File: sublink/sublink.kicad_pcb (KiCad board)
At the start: 2 copper layers, 21 parts

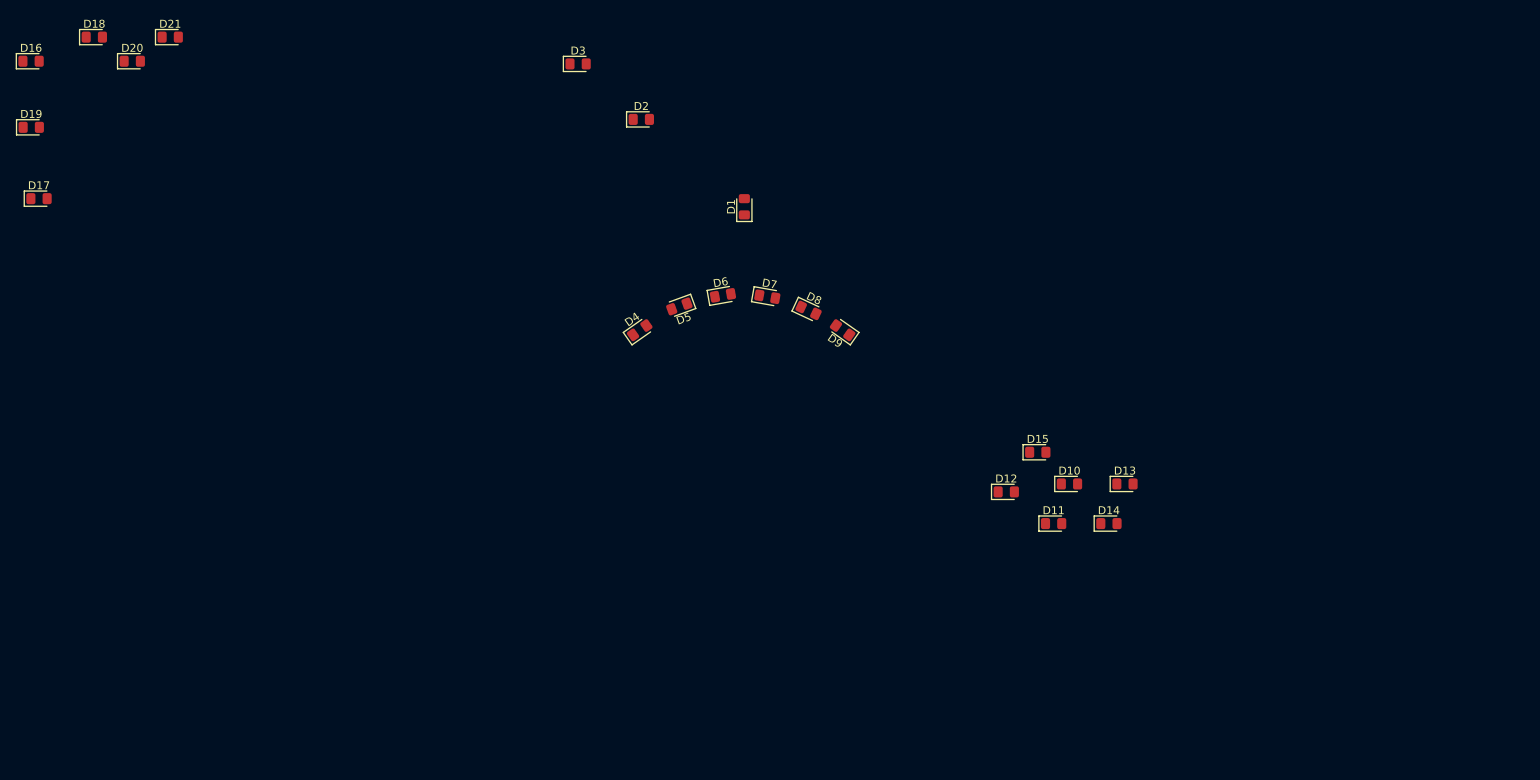
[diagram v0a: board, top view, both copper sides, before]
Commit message: wip board outline, led placement
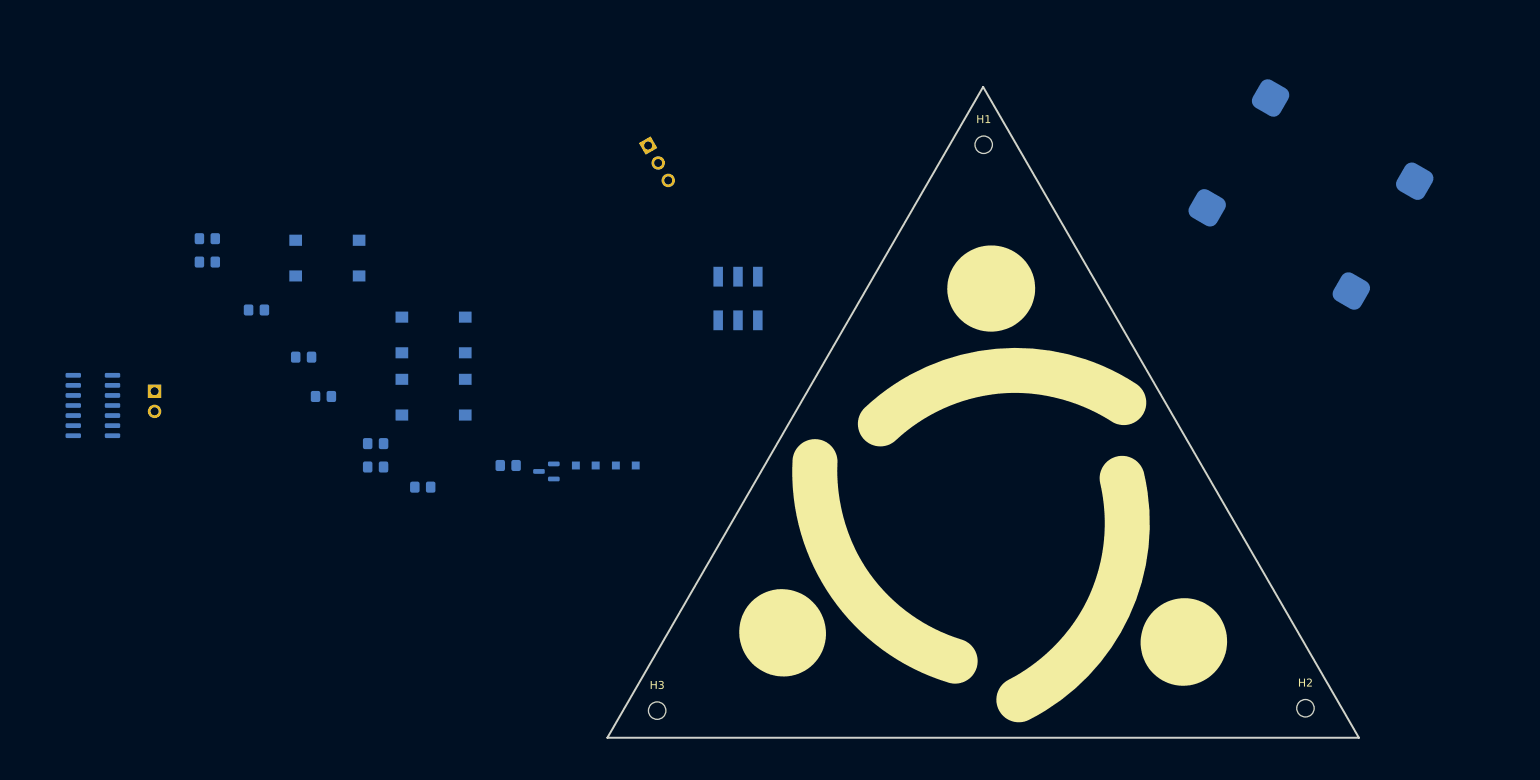
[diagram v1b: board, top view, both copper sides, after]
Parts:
- added BT1: 3V7, Connector_PinHeader_2.54mm:PinHeader_1x02_P2.54mm_Vertical, B.Cu at (68.6, 83.3)
- added D22: DNP, Diode_SMD:D_SOD-323_HandSoldering, B.Cu at (123.0, 92.7)
- added D23: BAS21HT1G, Diode_SMD:D_SOD-323_HandSoldering, B.Cu at (128.0, 92.7)
- added H1: MountingHole, MountingHole:MountingHole_2.2mm_M2, F.Cu at (173.2, 52.2)
- added H2: MountingHole, MountingHole:MountingHole_2.2mm_M2, F.Cu at (213.8, 123.3)
- added H3: MountingHole, MountingHole:MountingHole_2.2mm_M2, F.Cu at (132.0, 123.6)
- added J1: Conn_01x03_Female, Connector_PinSocket_2.54mm:PinSocket_1x03_P2.54mm_Horizontal, B.Cu at (130.9, 52.3)
- added Q1: YJL2305A, Package_TO_SOT_SMD:SOT-23, B.Cu at (118.0, 93.4)
- added R1: R_Small, Resistor_SMD:R_0805_2012Metric_Pad1.20x1.40mm_HandSolder, B.Cu at (75.2, 67.0)
- added R2: R_Small, Resistor_SMD:R_0805_2012Metric_Pad1.20x1.40mm_HandSolder, B.Cu at (96.5, 89.9)
- added R3: R_Small, Resistor_SMD:R_0805_2012Metric_Pad1.20x1.40mm_HandSolder, B.Cu at (102.4, 95.4)
- added R4: R_Small, Resistor_SMD:R_0805_2012Metric_Pad1.20x1.40mm_HandSolder, B.Cu at (113.2, 92.7)
- added R5: R_Small, Resistor_SMD:R_0805_2012Metric_Pad1.20x1.40mm_HandSolder, B.Cu at (89.9, 84.0)
- added R6: R_Small, Resistor_SMD:R_0805_2012Metric_Pad1.20x1.40mm_HandSolder, B.Cu at (75.2, 64.0)
- added R7: R_Small, Resistor_SMD:R_0805_2012Metric_Pad1.20x1.40mm_HandSolder, B.Cu at (81.4, 73.0)
- added R8: R_Small, Resistor_SMD:R_0805_2012Metric_Pad1.20x1.40mm_HandSolder, B.Cu at (96.5, 92.9)
- added R9: 10k, Resistor_SMD:R_0805_2012Metric_Pad1.20x1.40mm_HandSolder, B.Cu at (87.4, 79.0)
- added SW1: SW_Push, Button_Switch_SMD:SW_SPST_Omron_B3FS-100xP, B.Cu at (103.8, 76.2)
- added SW2: SW_Push, Button_Switch_SMD:SW_SPST_Omron_B3FS-100xP, B.Cu at (90.4, 66.5)
- added SW3: SW_Push, Button_Switch_SMD:SW_SPST_Omron_B3FS-100xP, B.Cu at (103.8, 84.0)
- added U1: ATtiny414-SS, Package_SO:SOIC-14_3.9x8.7mm_P1.27mm, B.Cu at (60.8, 85.1)
- added U2: OKY3402, sublink_custom:OKY3402, B.Cu at (214.5, 58.5)
- added U3: JS202011, sublink_custom:JS202011, B.Cu at (142.2, 71.6)
- moved D16 138.8 mm to (169.2, 117.6), turned to -20 degrees
- moved D17 122.7 mm to (163.3, 114.6), turned to -35 degrees
- moved D18 121.0 mm to (158.4, 110.4), turned to -50 degrees
- moved D19 115.5 mm to (154.7, 104.9), turned to -65 degrees
- moved D20 103.8 mm to (152.4, 98.9), turned to -80 degrees
- moved D21 97.3 mm to (151.7, 92.4), turned to -90 degrees
- moved D2 95.1 mm to (198.4, 115.0), turned to -25 degrees
- moved D3 76.2 mm to (147.8, 113.8), turned to -140 degrees
- moved D9 36.5 mm to (190.9, 84.2), turned to 150 degrees
- moved D8 34.8 mm to (184.8, 81.6), turned to 160 degrees
- moved D7 33.7 mm to (178.3, 80.7), turned to 180 degrees
- moved D6 33.1 mm to (171.9, 81.2), turned to -170 degrees
- moved D1 32.9 mm to (174.2, 70.3)
- moved D5 32.7 mm to (165.7, 83.4), turned to -155 degrees
- moved D4 32.6 mm to (160.3, 87.1), turned to -140 degrees
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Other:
- board outline added: 94.8 x 82.1 mm

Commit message: first pass all components placement
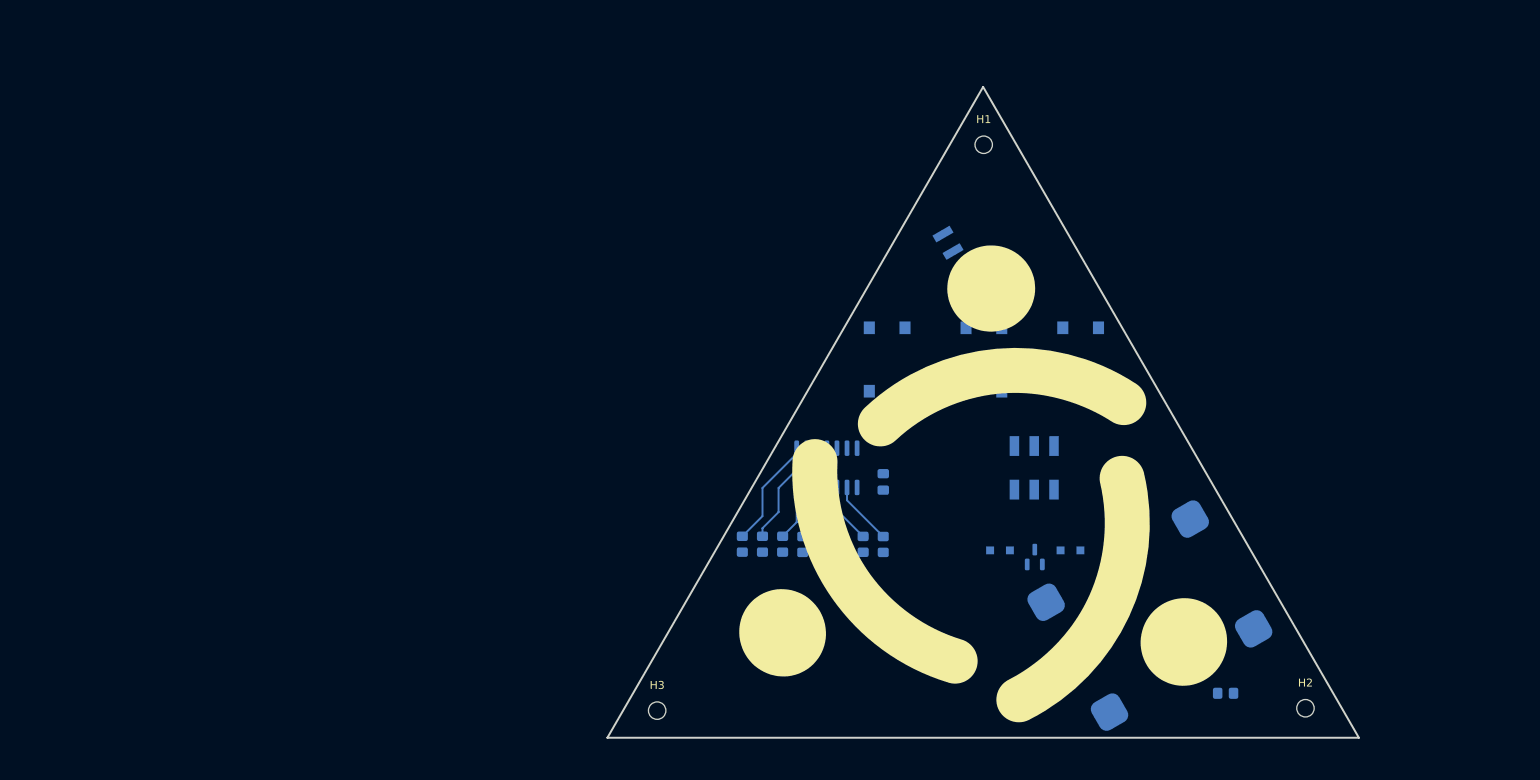
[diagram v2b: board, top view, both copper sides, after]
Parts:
- added C1: 100n, Capacitor_SMD:C_0805_2012Metric_Pad1.18x1.45mm_HandSolder, B.Cu at (160.5, 94.7)
- J1: value Conn_01x03_Female -> ZL315-4SGH; footprint Connector_PinSocket_2.54mm:PinSocket_1x03_P2.54mm_Horizontal -> Connector_Harwin:Harwin_M20-89004xx_1x04_P2.54mm_Horizontal
- moved R9 123.8 mm to (203.7, 121.4)
- moved BT1 117.6 mm to (180.6, 119.1)
- moved U1 92.9 mm to (153.4, 93.0), turned to 90 degrees
- moved R6 91.3 mm to (158.0, 102.6), turned to 90 degrees
- moved SW2 83.8 mm to (173.2, 79.3), turned to 90 degrees
- moved SW3 81.8 mm to (185.4, 79.3), turned to 90 degrees
- moved R7 79.7 mm to (155.4, 102.6), turned to 90 degrees
- moved R1 78.6 mm to (145.3, 102.6), turned to -90 degrees
- moved R5 73.1 mm to (160.5, 102.6), turned to 90 degrees
- moved Q1 62.6 mm to (179.6, 104.2), turned to 90 degrees
- moved D22 62.1 mm to (184.2, 103.4), turned to 0 degrees
- moved SW1 57.3 mm to (161.0, 79.3), turned to 90 degrees
- moved R8 57.3 mm to (152.9, 102.6), turned to 90 degrees
- moved U2 56.9 mm to (194.2, 111.6), turned to 120 degrees
- moved D23 48.4 mm to (175.3, 103.4)
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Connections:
- J1 pad 1: GND -> Net-(U3-Pad3)
- J1 pad 3: Net-(J1-Pad3) -> GND
- U1 pad 11: butt2 -> butt1
- U1 pad 12: butt3 -> butt2
- U1 pad 13: Net-(R4-Pad2) -> butt3
- U1 pad 6: butt1 -> Net-(R4-Pad2)
- U3 pad 3: Net-(J1-Pad3) -> Net-(U3-Pad3)
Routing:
- net Net-(R2-Pad1): track 0.00 -> 14.0 mm
- net Net-(R1-Pad1): track 0.00 -> 13.4 mm
- net Net-(R5-Pad2): track 0.00 -> 8.09 mm
- net Net-(R6-Pad2): track 0.00 -> 7.54 mm
- net Net-(R7-Pad2): track 0.00 -> 7.03 mm
- net Net-(R3-Pad1): track 0.00 -> 6.90 mm
- net Net-(R8-Pad2): track 0.00 -> 6.51 mm
- net Net-(R4-Pad2): track 0.00 -> 6.40 mm
- net UPDI: track 0.00 -> 0.51 mm
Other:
- board text added: "21x38.5mm"
- board text added: "BATT"
- board text added: "JST batt connector mated assembly (23.3 x 6.3 x 3.2)"
- board text added: "aint nobody got space for that!"

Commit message: wip routing
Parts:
- BT1: footprint Connector_PinHeader_2.54mm:PinHeader_1x02_P2.54mm_Vertical -> Resistor_SMD:R_1206_3216Metric_Pad1.30x1.75mm_HandSolder
- Q1: value YJL2305A -> Q_PMOS_GSD
- moved D23 26.9 mm to (202.1, 102.1), turned to -90 degrees
- moved R9 22.7 mm to (181.0, 121.4), turned to 90 degrees
- moved Q1 15.9 mm to (195.4, 101.8), turned to 0 degrees
- moved D22 15.1 mm to (199.2, 102.0), turned to -90 degrees
- moved BT1 11.7 mm to (180.3, 107.5)
- moved U2 4.67 mm to (195.6, 116.1), turned to 90 degrees
- moved U3 0.50 mm to (179.5, 92.5)
- turned SW1 to -90 degrees
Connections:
- J1 pad 1: Net-(U3-Pad3) -> Net-(U3-Pad1)
- Q1 pad 1: Net-(BT1-Pad1) -> Net-(D23-Pad2)
- Q1 pad 2: Net-(D23-Pad2) -> Net-(D22-Pad1)
- Q1 pad 3: Net-(D22-Pad1) -> Net-(BT1-Pad1)
- U3 pad 1: Net-(D22-Pad1) -> Net-(U3-Pad1)
- U3 pad 2: unconnected-(U3-Pad2) -> VCC
- U3 pad 3: Net-(U3-Pad3) -> unconnected-(U3-Pad3)
- U3 pad 6: unconnected-(U3-Pad6) -> Net-(D22-Pad1)
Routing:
- net Net-(D23-Pad2): track 0.00 -> 42.2 mm
- net butt3: track 0.00 -> 38.5 mm
- net Net-(U3-Pad1): track 0.00 -> 36.5 mm
- net UPDI: track 0.51 -> 35.6 mm
- net butt2: track 0.00 -> 29.4 mm
- net VCC: track 0.00 -> 29.3 mm
- net Net-(D22-Pad1): track 0.00 -> 24.8 mm
- net Net-(BT1-Pad1): track 0.00 -> 22.2 mm
- net butt1: track 0.00 -> 21.8 mm
- net GND: track 0.00 -> 9.39 mm

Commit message: wip top radial routing
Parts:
- removed U2: OKY3402, sublink_custom:OKY3402
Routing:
- net L2: track 0.00 -> 96.8 mm, vias 0 -> 4
- net L1: track 0.00 -> 85.3 mm, vias 0 -> 4
- net L3: track 0.00 -> 82.1 mm, vias 0 -> 3
- net L0: track 0.00 -> 61.6 mm, vias 0 -> 2
- net L4: track 0.00 -> 60.8 mm, vias 0 -> 2

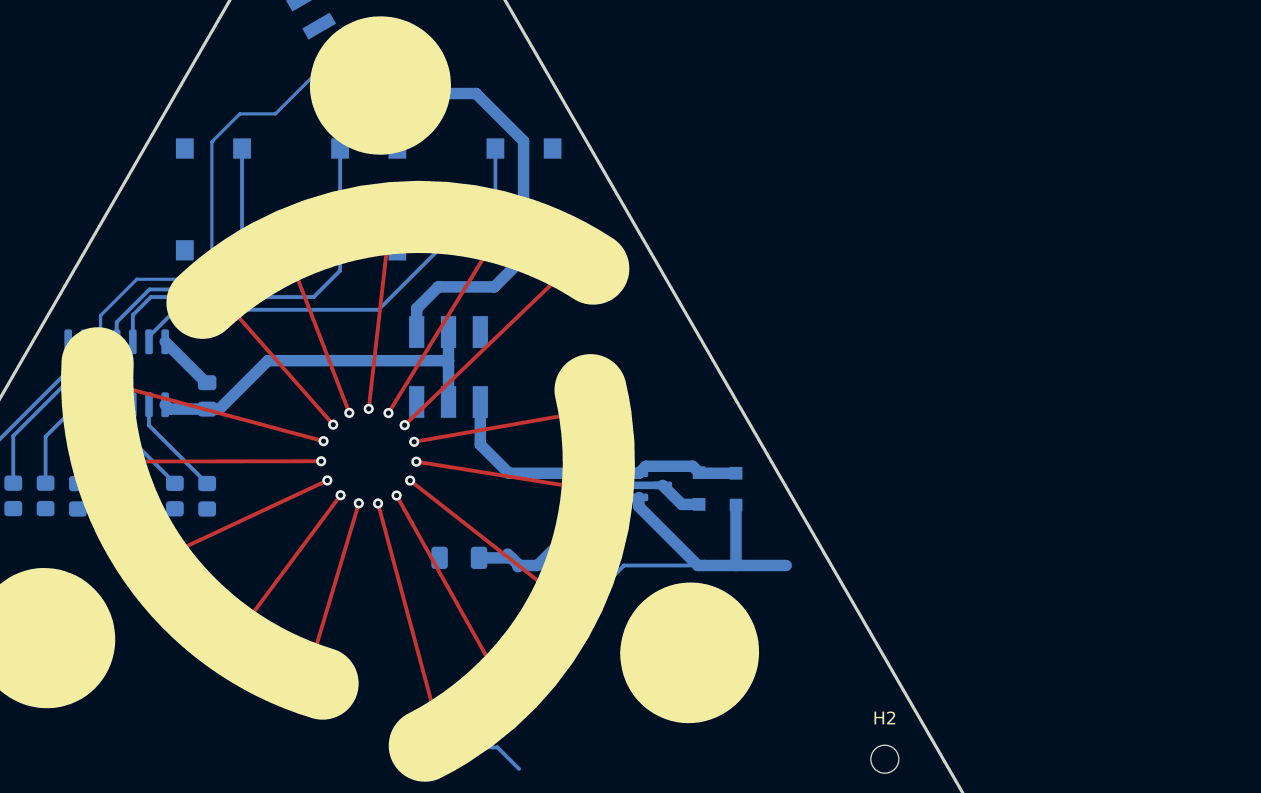
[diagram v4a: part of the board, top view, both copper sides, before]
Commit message: bottom circle routing. Broke chargin part footprint for some reason
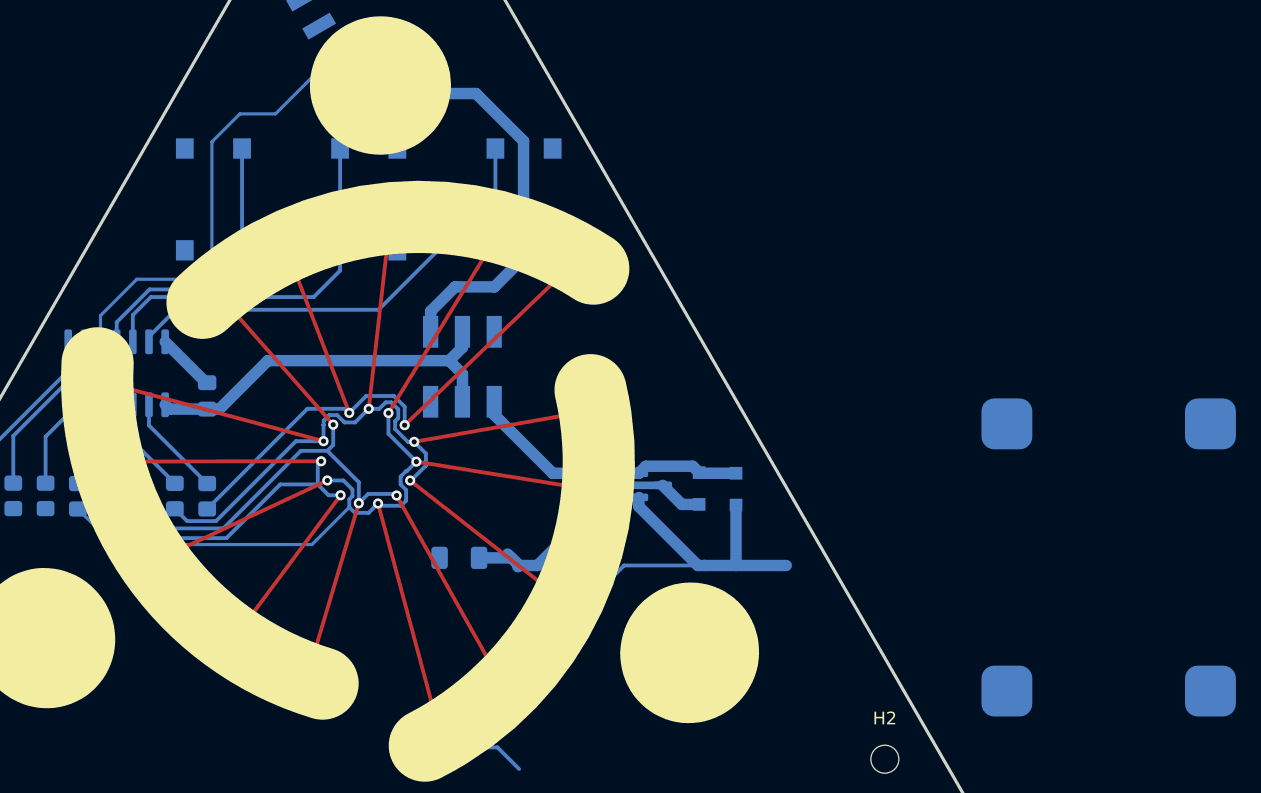
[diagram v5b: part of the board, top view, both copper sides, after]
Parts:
- added U2: OKY3402, sublink_custom:OKY3402, B.Cu at (231.4, 107.4)
- moved U3 1.09 mm to (180.6, 92.5)
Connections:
- J1 pad 1: Net-(U3-Pad1) -> Net-(J1-Pad1)
- R4 pad 1: L0 -> L2
- R5 pad 1: L1 -> L0
- R6 pad 1: L2 -> L1
- U3 pad 1: Net-(U3-Pad1) -> unconnected-(U3-Pad1)
- U3 pad 3: unconnected-(U3-Pad3) -> Net-(J1-Pad1)
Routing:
- net L2: track 96.8 -> 138.0 mm
- net Net-(U3-Pad1): track 36.5 -> 0.00 mm
- net unconnected-(U3-Pad1): track 0.00 -> 35.3 mm
- net L1: track 85.3 -> 116.3 mm
- net L3: track 82.1 -> 110.5 mm
- net L4: track 60.8 -> 83.9 mm
- net L0: track 61.6 -> 82.9 mm
- net Net-(D22-Pad1): track 24.8 -> 22.4 mm
- net VCC: track 29.5 -> 30.4 mm
